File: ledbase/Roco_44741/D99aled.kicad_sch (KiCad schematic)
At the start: 76 parts, among them U1 74HC595, U2 74HC595, U3 74HC595, U4 74HC595, U5 MCP6001x-LT

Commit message: add: ledbase Roco_44741
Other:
- title: Coach LED carrier PCB -> LED base: Roco #44741
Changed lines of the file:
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@@
 	(paper "A4")
 	(title_block
-		(title "Coach LED carrier PCB")
-		(date "2025-02-18")
-		(rev "0")
+		(title "LED base: Roco #44741")
+		(date "2025-10-19")
+		(rev "1")
 		(company "Frank Schumacher")
 		(comment 1 "D99a")
-		(comment 2 "Prototype 1")
+		(comment 2 "Prototype")
 	)
 	(text "#2"

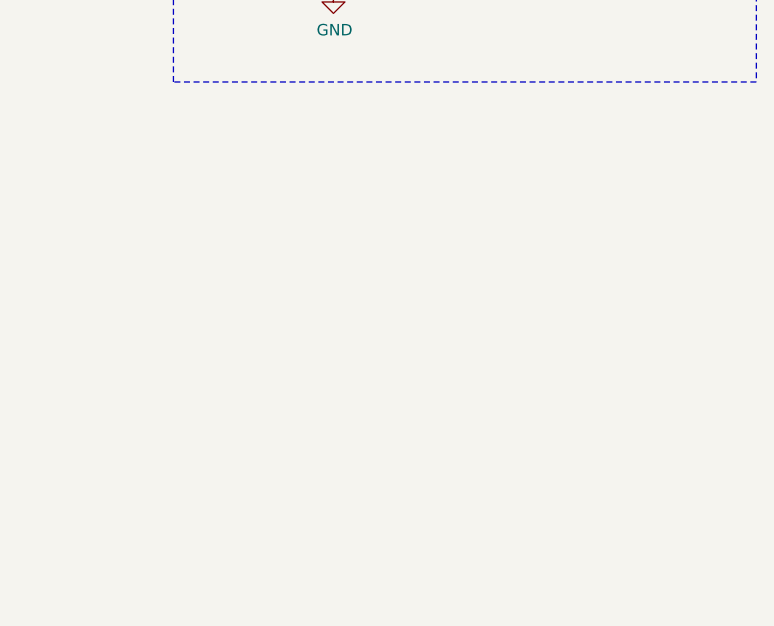
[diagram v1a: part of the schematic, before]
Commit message: mod: ncap leakage resistor
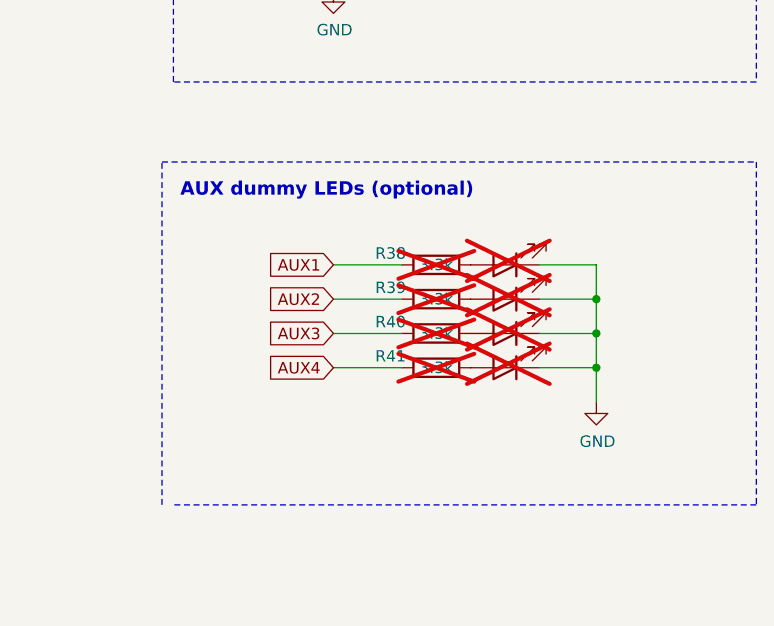
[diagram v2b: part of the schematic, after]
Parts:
- added D34, D35, D36, D37: LED, LED_SMD:LED_0603_1608Metric, symbol Device:LED
- added R38, R39, R40, R41: 3.3k, Resistor_SMD:R_0603_1608Metric, symbol Device:R
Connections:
- net GND: now also D34.1 (K), D35.1 (K), D36.1 (K), D37.1 (K)
- new net: D35.2 (A), R39.2
- new net: D37.2 (A), R41.2
- new net: D34.2 (A), R38.2
- new net: D36.2 (A), R40.2
- new net AUX1: R38.1
- new net AUX2: R39.1
- new net AUX3: R40.1
- new net AUX4: R41.1
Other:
- note added: "AUX dummy LEDs (optional)"
